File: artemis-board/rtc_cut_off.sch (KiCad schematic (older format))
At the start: 15 parts, among them Q10 AO3401A, Q11 2N7002, Q3 2N7002, U5 PCA9557PW, U7 PCF8563T, Y2 32.768KHz

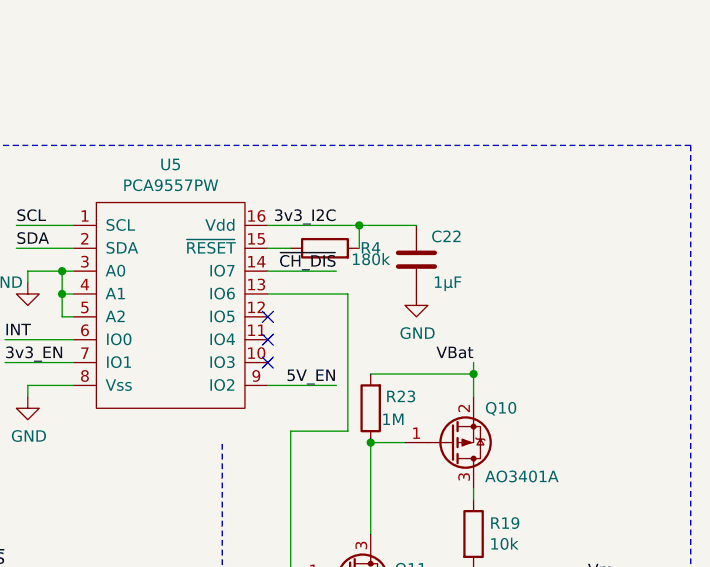
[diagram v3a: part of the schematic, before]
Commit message: added reverse polarity protection to power input
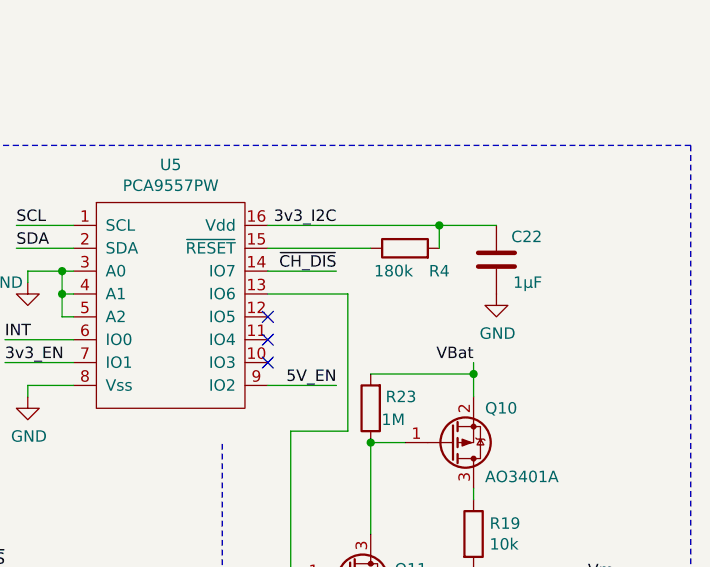
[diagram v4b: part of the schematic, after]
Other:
- moved on the sheet: C22, R4
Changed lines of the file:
@@
 L Device:C C22
 U 1 1 5FC9C8EC
-P 5450 1850
-F 0 "C22" H 5250 1750 50  0000 L CNN
-F 1 "1µF" H 5250 1950 50  0000 L CNN
-F 2 "Capacitor_SMD:C_0603_1608Metric_Pad1.08x0.95mm_HandSolder" H 5488 1700 50  0001 C CNN
-F 3 "~" H 5450 1850 50  0001 C CNN
-F 4 "C15849" H 5450 1850 50  0001 C CNN "LCSC"
-	1    5450 1850
+P 5800 1850
+F 0 "C22" H 5600 1750 50  0000 L CNN
+F 1 "1µF" H 5600 1950 50  0000 L CNN
+F 2 "Capacitor_SMD:C_0603_1608Metric_Pad1.08x0.95mm_HandSolder" H 5838 1700 50  0001 C CNN
+F 3 "~" H 5800 1850 50  0001 C CNN
+F 4 "C15849" H 5800 1850 50  0001 C CNN "LCSC"
+	1    5800 1850
 	-1   0    0    1
 $EndComp
@@
 L power:GND #PWR0110
 U 1 1 5FCA03ED
-P 5450 2000
-F 0 "#PWR0110" H 5450 1750 50  0001 C CNN
-F 1 "GND" H 5455 1827 50  0000 C CNN
-F 2 "" H 5450 2000 50  0001 C CNN
-F 3 "" H 5450 2000 50  0001 C CNN
-	1    5450 2000
+P 5800 2000
+F 0 "#PWR0110" H 5800 1750 50  0001 C CNN
+F 1 "GND" H 5805 1827 50  0000 C CNN
+F 2 "" H 5800 2000 50  0001 C CNN
+F 3 "" H 5800 2000 50  0001 C CNN
+	1    5800 2000
 	1    0    0    -1
 $EndComp
@@
 L Device:R R4
 U 1 1 5FC6F3D4
-P 5050 1800
-F 0 "R4" V 5050 1600 50  0000 C CNN
-F 1 "180k" V 5000 1600 50  0000 C CNN
-F 2 "Resistor_SMD:R_0603_1608Metric_Pad1.05x0.95mm_HandSolder" V 4980 1800 50  0001 C CNN
-F 3 "~" H 5050 1800 50  0001 C CNN
-F 4 "C22827" H 5050 1800 50  0001 C CNN "LCSC"
-	1    5050 1800
+P 5400 1800
+F 0 "R4" V 5300 1650 50  0000 C CNN
+F 1 "180k" V 5300 1850 50  0000 C CNN
+F 2 "Resistor_SMD:R_0603_1608Metric_Pad1.05x0.95mm_HandSolder" V 5330 1800 50  0001 C CNN
+F 3 "~" H 5400 1800 50  0001 C CNN
+F 4 "C22827" H 5400 1800 50  0001 C CNN "LCSC"
+	1    5400 1800
 	0    -1   -1   0
 $EndComp
 Wire Wire Line
-	4800 1800 4900 1800
-Wire Wire Line
-	5200 1700 5200 1800
-Wire Wire Line
-	4800 1700 5200 1700
-Wire Wire Line
-	5450 1700 5200 1700
-Connection ~ 5200 1700
+	4800 1800 5250 1800
+Wire Wire Line
+	5550 1700 5550 1800
+Wire Wire Line
+	4800 1700 5550 1700
+Wire Wire Line
+	5800 1700 5550 1700
+Connection ~ 5550 1700
 Wire Notes Line
 	4600 3900 4600 2650
